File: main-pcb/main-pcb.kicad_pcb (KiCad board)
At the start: 10 copper layers, 118 x 90 mm, 443 parts, among them J1 CONN_01X03, J10 CONN_DUMPTRUCK_HOST, J11 CONN_01X03, J12 PMOD_HOST, J13 PMOD_HOST, J14 USB_C_Receptacle_USB2.0, J2 CORTEX_DEBUG_ETM, J3 XILINX_JTAG, J4 CORTEX_DEBUG_ETM, J5 CONN_01X03, J6 0826-1G1T-23-F, J7 CONN_DUMPTRUCK_HOST, J8 CONN_DUMPTRUCK_HOST, J9 CONN_DUMPTRUCK_HOST, M1 MECHANICAL, M2 SCREWHOLE, M3 SCREWHOLE, M4 SCREWHOLE, M5 SCREWHOLE, M6 MECHANICAL, M7 MECHANICAL, M8 MECHANICAL, M9 MECHANICAL, Q1 SSM6N58NU, SW1 SWITCH, SW2 SWITCH, U1 XC7S100-1FGGA484C, U10 NCP45525IMNTWG-H, U11 LTC3374-QFN, U12 AT24MAC402, U13 ECS-1612MV-250-CN, U14 STM32H735-UFBGA176-25, U15 S27KL0642GABHB020, U16 ECS-1612MV-250-CN, U17 S27KS0642GABHI030, U18 ECS-1612MV-250-CN, U19 INA230, U2 STM32L431-QFN48, U20 KSZ9031RN, U21 RCLAMP0514M, U22 RCLAMP0514M, U23 NCP45525IMNTWG-H, U24 IS25WP256D-JLLE, U25 INA230, U26 74LVC1T45, U27 NCP45525IMNTWG-H, U28 INA230, U29 NCP45525IMNTWG-H, U3 INA230, U30 INA230, U31 NCP45525IMNTWG-H, U32 INA230, U33 19-C47/RSGHBHC-5V01/2T, U34 19-C47/RSGHBHC-5V01/2T, U35 19-C47/RSGHBHC-5V01/2T, U36 19-C47/RSGHBHC-5V01/2T, U37 19-C47/RSGHBHC-5V01/2T, U38 19-C47/RSGHBHC-5V01/2T, U39 NCP45525IMNTWG-H, U4 INA230, U5 INA230, U6 INA230, U7 INA230, U8 INA230, U9 INA230

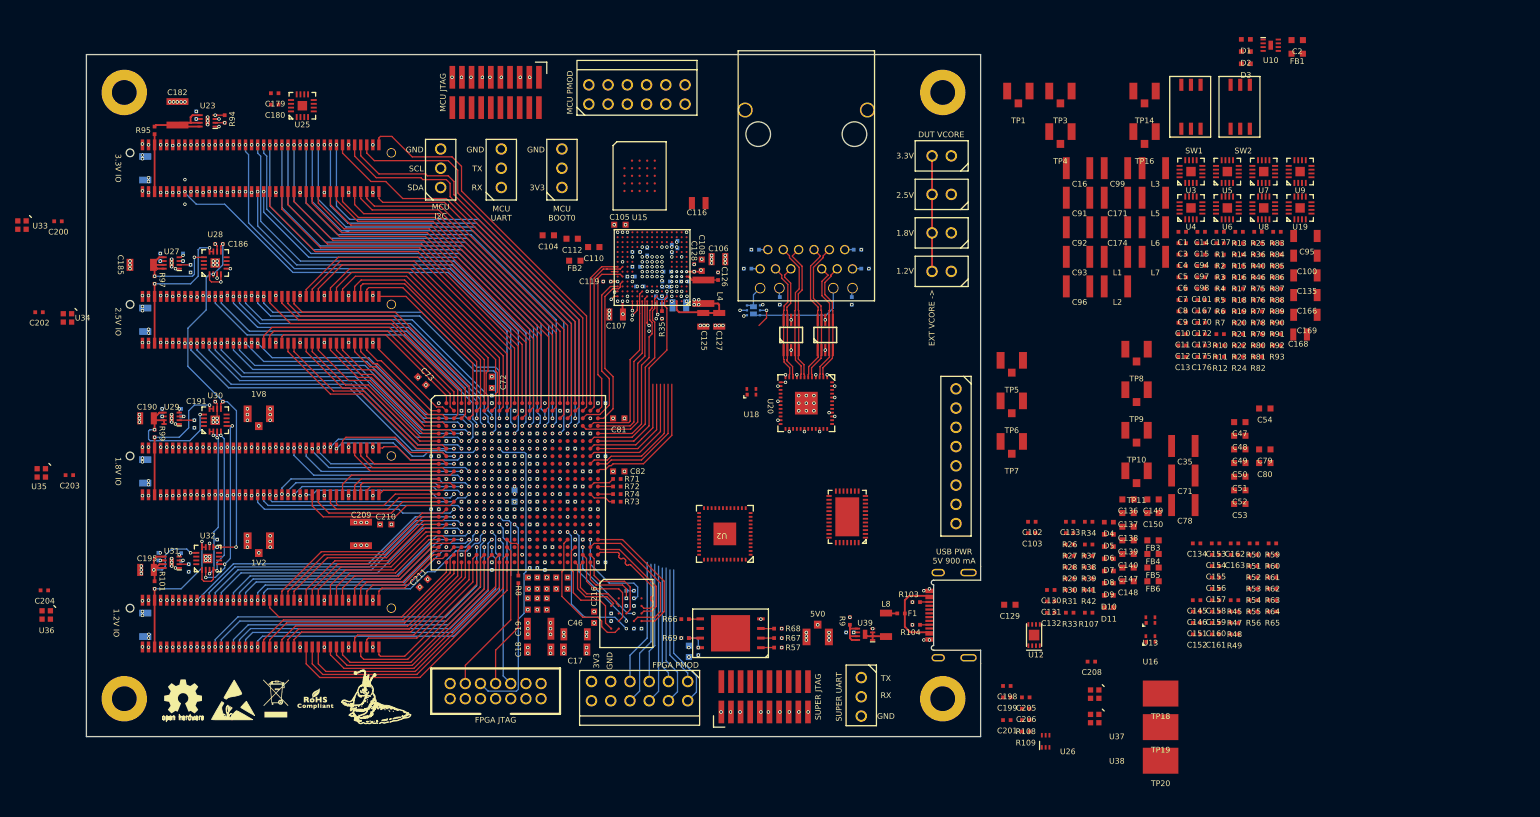
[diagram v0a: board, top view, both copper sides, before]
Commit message: Continued routing MCU, started work on PHY
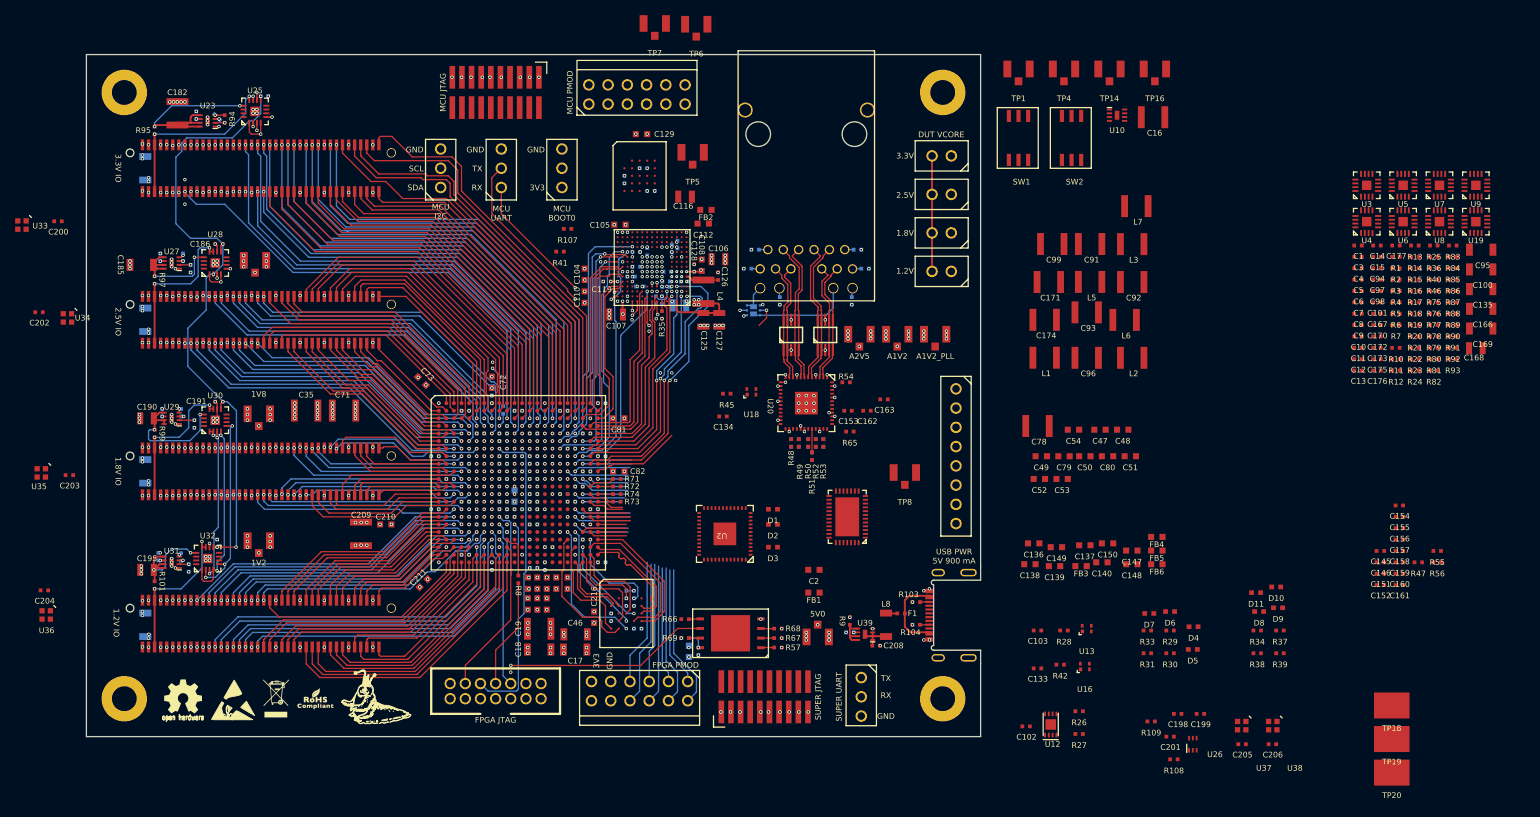
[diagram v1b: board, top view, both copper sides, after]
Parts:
- added R110: 33, azonenberg_pcb:EIA_0402_RES_NOSILK, B.Cu at (92.0, 72.9)
- C130, C131, C132, C179, C180, R59, R60, R61, R62, R63, R64: moved to B.Cu
- moved C35 115.8 mm to (66.0, 73.0), turned to 180 degrees
- moved C71 111.1 mm to (71.0, 73.0), turned to 180 degrees
- moved TP3 108.6 mm to (59.2, 53.2)
- moved FB1 95.5 mm to (133.0, 97.0)
- moved C2 94.6 mm to (133.0, 94.0)
- moved D3 89.2 mm to (127.6, 91.0)
- moved D2 88.2 mm to (127.6, 88.0)
- moved D1 88.0 mm to (127.6, 86.0)
- moved R107 85.4 mm to (100.5, 49.0)
- moved R41 82.0 mm to (99.5, 52.0)
- moved C131 79.1 mm to (108.0, 42.5), turned to 90 degrees
- moved C129 78.9 mm to (110.2, 36.5)
- moved C130 77.4 mm to (110.5, 41.0), turned to 180 degrees
- moved C132 76.7 mm to (111.5, 44.0)
- moved TP7 72.5 mm to (112.0, 22.0)
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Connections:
- U1 pad D9: /FLASH_SCK -> Net-(U1A-CCLK_0)
- U1 pad F17: /MCU/FMC_AD7 -> /MCU/FMC_AD11
- U1 pad F18: /MCU/FMC_NOE -> /MCU/FMC_AD14
- U1 pad F20: /MCU/FMC_AD13 -> /MCU/FMC_AD10
- U1 pad G17: /MCU/FMC_NBL0 -> /MCU/FMC_A17
- U1 pad G20: /MCU/FMC_A25 -> /MCU/FMC_AD13
- U1 pad G21: /MCU/FMC_A17 -> /MCU/FMC_NBL0
- U1 pad G22: /MCU/FMC_AD9 -> /MCU/FMC_A23
- U1 pad H18: /MCU/FMC_AD11 -> /MCU/FMC_AD7
- U1 pad H19: /MCU/FMC_AD10 -> /MCU/FMC_AD15
- U1 pad H20: /MCU/FMC_AD14 -> /MCU/FMC_NOE
- U1 pad H21: /MCU/FMC_AD15 -> /MCU/FMC_A19
- U1 pad J16: /MCU/FMC_A19 -> /MCU/FMC_A25
- U1 pad J19: /MCU/FMC_A20 -> /MCU/FMC_A22
- U1 pad J20: /MCU/FMC_A21 -> /MCU/FMC_AD9
- U1 pad J21: /MCU/FMC_A22 -> /MCU/FMC_A20
- U1 pad J22: /MCU/FMC_A23 -> /MCU/FMC_A21
- U1 pad P15: /Ethernet/ETH_MDIO -> unconnected-(U1E-IO_L13P_T2_MRCC_14-PadP15)
- U1 pad P16: /Ethernet/ETH_MDC -> unconnected-(U1E-IO_L13N_T2_MRCC_14-PadP16)
- U1 pad P17: /Ethernet/ETH_RST_N -> unconnected-(U1E-IO_L14P_T2_SRCC_14-PadP17)
- U1 pad R17: /Ethernet/ETH_LED2_N_1V8_INV -> unconnected-(U1E-IO_L16N_T2_D31_14-PadR17)
- U1 pad R18: unconnected-(U1E-IO_L14N_T2_SRCC_14-PadR18) -> /Ethernet/ETH_MDC
- U1 pad T19: unconnected-(U1E-IO_L18P_T2_D28_14-PadT19) -> /Ethernet/ETH_RST_N
- U1 pad T20: unconnected-(U1E-IO_L18N_T2_D27_14-PadT20) -> /Ethernet/ETH_LED2_N_1V8_INV
- U1 pad U17: /Ethernet/ETH_LED2_N_1V8 -> unconnected-(U1E-IO_L15N_T2_DQS_DOUT_CSO_B_14-PadU17)
- U1 pad U19: unconnected-(U1E-IO_L12N_T1_MRCC_14-PadU19) -> /Ethernet/ETH_MDIO
- U1 pad U20: unconnected-(U1E-IO_L11P_T1_SRCC_14-PadU20) -> /Ethernet/ETH_LED2_N_1V8
- U14 pad F15: /MCU/MCU_PMOD_DQ6 -> unconnected-(U14G-PG5-PadF15)
- U14 pad G12: /MCU/MCU_PMOD_DQ0 -> unconnected-(U14G-PG8-PadG12)
- U14 pad G13: /MCU/MCU_PMOD_DQ4 -> unconnected-(U14G-PG7-PadG13)
- U14 pad G14: /MCU/MCU_PMOD_DQ5 -> unconnected-(U14G-PG4-PadG14)
- U14 pad G15: /MCU/MCU_HYPERRAM_RST_N -> unconnected-(U14G-PG2-PadG15)
- U14 pad P10: unconnected-(U14B-PB11-PadP10) -> /MCU/MCU_PMOD_DQ0
- U14 pad P12: unconnected-(U14E-PE12-PadP12) -> /MCU/MCU_PMOD_DQ4
- U14 pad P13: unconnected-(U14E-PE13-PadP13) -> /MCU/MCU_PMOD_DQ5
- U14 pad R7: unconnected-(U14A-PA6-PadR7) -> /MCU/MCU_HYPERRAM_RST_N
- U14 pad R8: unconnected-(U14B-PB0-PadR8) -> /MCU/MCU_PMOD_DQ6
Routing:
- net /3V3: track 323.8 -> 442.5 mm, vias 45 -> 52
- net /GND: track 1304.7 -> 1400.8 mm, vias 388 -> 443
- net /FLASH_SCK: track 0.00 -> 72.9 mm, vias 1 -> 2
- net /MCU/FMC_A21: track 0.00 -> 36.1 mm, vias 1 -> 2
- net /MCU/FMC_A20: track 0.05 -> 33.6 mm, vias 1 -> 2
- net /3V3_SB: track 50.9 -> 84.0 mm, vias 7 -> 8
- net /MCU/FMC_AD11: track 0.00 -> 32.9 mm, vias 0 -> 2
- net /MCU/FMC_AD14: track 0.00 -> 30.9 mm, vias 0 -> 2
- net /MCU/FMC_AD13: track 0.00 -> 30.6 mm, vias 0 -> 2
- net /MCU/FMC_A19: track 0.05 -> 29.6 mm, vias 1 -> 2
- net /MCU/FMC_AD10: track 0.00 -> 28.8 mm, vias 0 -> 2
- net /MCU/FMC_NBL0: track 0.00 -> 27.9 mm
- net /SUPER_I2C_SDA: track 50.4 -> 78.3 mm, vias 4 -> 5
- net /MCU/MCU_UART_TX: track 1.02 -> 28.1 mm, vias 1 -> 2
- net /MCU/FMC_NOE: track 0.00 -> 26.7 mm, vias 1 -> 2
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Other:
- board text added: "A1V2"
- board text added: "A1V2_PLL"
- board text added: "A2V5"
- board text added: "FPGA"
- board text added: "LTC3374"
- board text added: "PHY"
- board text added: "Power infra"
- board text removed: "EXT VCORE ->"

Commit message: Continued routing MCU
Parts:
- C112, FB2, R107, R34, R37, R38, R39, R41: moved to B.Cu
- moved R39 112.0 mm to (104.2, 38.8)
- moved R38 108.9 mm to (104.2, 40.0)
- moved R37 108.9 mm to (104.2, 41.2)
- moved D9 106.1 mm to (105.2, 41.2), turned to 180 degrees
- moved R34 105.7 mm to (104.1, 42.5)
- moved D10 105.1 mm to (105.2, 40.0), turned to 180 degrees
- moved D11 104.0 mm to (105.2, 38.8), turned to 180 degrees
- moved D8 103.6 mm to (105.2, 42.5), turned to 180 degrees
- moved TP6 33.9 mm to (98.5, 50.2)
- moved C116 20.3 mm to (95.8, 46.7)
- moved TP7 20.0 mm to (117.2, 41.2)
- moved R41 16.3 mm to (110.0, 39.5), turned to -90 degrees
- moved R107 14.2 mm to (111.0, 39.5), turned to -90 degrees
- moved C112 3.32 mm to (115.2, 47.2), turned to 90 degrees
- moved TP5 2.51 mm to (117.2, 36.5)
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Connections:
- U1 pad G16: /MCU/FMC_AD8 -> /MCU/FMC_AD6
- U1 pad H18: /MCU/FMC_AD7 -> /MCU/FMC_AD9
- U1 pad J15: /MCU/FMC_AD1 -> /MCU/FMC_AD7
- U1 pad J16: /MCU/FMC_A25 -> /MCU/FMC_AD8
- U1 pad J17: /MCU/FMC_NBL1 -> /MCU/FMC_AD12
- U1 pad J19: /MCU/FMC_A22 -> /MCU/FMC_NBL1
- U1 pad J20: /MCU/FMC_AD9 -> /MCU/FMC_A16
- U1 pad K18: /MCU/FMC_AD12 -> /MCU/FMC_A25
- U1 pad K19: /MCU/FMC_AD6 -> /MCU/FMC_A22
- U1 pad K22: /MCU/FMC_A16 -> /MCU/FMC_AD1
- U14 pad L15: unconnected-(U14B-PB13-PadL15) -> /MCU/MCU_PMOD_DQ4
- U14 pad M1: /MCU/MCU_LED_0 -> unconnected-(U14C-PC2-PadM1)
- U14 pad M15: /MCU/MCU_PMOD_DQ2 -> /MCU/MCU_PMOD_DQ0
- U14 pad M2: unconnected-(U14C-PC3-PadM2) -> /PRSNT_1V2
- U14 pad M7: /MCU/MCU_PMOD_DQ3 -> unconnected-(U14C-PC5-PadM7)
- U14 pad N12: unconnected-(U14B-PB10-PadN12) -> /MCU/MCU_LED_3
- U14 pad N13: unconnected-(U14H-PH8-PadN13) -> /MCU/MCU_LED_0
- U14 pad N14: unconnected-(U14H-PH10-PadN14) -> /MCU/MCU_PMOD_DQ5
- U14 pad N15: /MCU/MCU_LED_2 -> /MCU/MCU_PMOD_DQ1
- U14 pad P10: /MCU/MCU_PMOD_DQ0 -> unconnected-(U14B-PB11-PadP10)
- U14 pad P11: /MCU/MCU_LED_1 -> unconnected-(U14F-PF12-PadP11)
- U14 pad P12: /MCU/MCU_PMOD_DQ4 -> /MCU/MCU_LED_2
- U14 pad P13: /MCU/MCU_PMOD_DQ5 -> /MCU/MCU_LED_1
- U14 pad P15: /MCU/MCU_LED_3 -> /MCU/MCU_PMOD_DQ6
- U14 pad P5: /PRSNT_1V2 -> /MCU/MCU_PMOD_DQ3
- U14 pad R10: /MCU/MCU_PMOD_DQ1 -> unconnected-(U14F-PF14-PadR10)
- U14 pad R4: unconnected-(U14H-PH3-PadR4) -> /MCU/MCU_PMOD_DQ7
- U14 pad R6: /MCU/MCU_PMOD_DQ7 -> /MCU/MCU_PMOD_DQ2
- U14 pad R8: /MCU/MCU_PMOD_DQ6 -> unconnected-(U14B-PB0-PadR8)
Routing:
- net /3V3_SB: track 84.0 -> 174.5 mm, vias 8 -> 10
- net /1V8: track 172.5 -> 247.7 mm
- net /GND: track 1400.8 -> 1466.1 mm, vias 443 -> 474
- net /2V5: track 98.3 -> 160.9 mm
- net /3V3: track 442.5 -> 503.3 mm, vias 52 -> 57
- net Net-(J11-P2): track 0.00 -> 47.3 mm, vias 0 -> 1
- net /MCU/FMC_AD5: track 0.00 -> 47.2 mm, vias 1 -> 2
- net /MCU/FMC_AD7: track 0.00 -> 46.8 mm, vias 1 -> 2
- net /MCU/FMC_AD4: track 0.00 -> 43.0 mm, vias 1 -> 2
- net /MCU/FMC_AD8: track 0.00 -> 40.9 mm, vias 1 -> 2
- net /MCU/MCU_RST_N: track 0.00 -> 38.5 mm, vias 0 -> 3
- net /MCU/MCU_JTAG_TDO: track 11.8 -> 49.8 mm, vias 1 -> 2
- net /MCU/FMC_AD9: track 6.50 -> 43.1 mm, vias 1 -> 2
- net /I2C_SDA: track 126.8 -> 161.7 mm, vias 4 -> 5
- net /MCU/FMC_A25: track 0.00 -> 33.9 mm
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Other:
- board text added: "2V5"
- board text added: "VCORE"
- board text added: "VDDA"
- board text added: "VSMPS"

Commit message: 500 unrouted, still lots more to go
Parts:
- C103, C145, C146, C151, C152, C153, C154, C156, C157, C158, C159, C160, C161, C162, C163, R26, R27: moved to B.Cu
- moved R27 129.3 mm to (70.8, 30.5), turned to 90 degrees
- moved R26 127.7 mm to (69.8, 31.0), turned to 90 degrees
- moved C102 124.5 mm to (68.5, 31.2), turned to 180 degrees
- moved U12 124.4 mm to (69.8, 33.5)
- moved C160 84.6 mm to (128.8, 71.8)
- moved C158 84.1 mm to (129.2, 68.8), turned to -90 degrees
- moved C157 83.0 mm to (128.8, 74.2)
- moved C151 81.8 mm to (129.5, 70.8)
- moved C159 80.7 mm to (133.2, 68.8), turned to -90 degrees
- moved C152 80.5 mm to (130.0, 75.2), turned to 90 degrees
- moved C161 79.5 mm to (135.2, 69.8), turned to 180 degrees
- moved C146 78.3 mm to (131.5, 75.4), turned to 90 degrees
- moved C156 77.3 mm to (134.5, 73.2), turned to 180 degrees
- moved C154 76.3 mm to (135.2, 71.2), turned to 180 degrees
- moved C145 75.8 mm to (133.8, 75.3), turned to 90 degrees
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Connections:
- R65 pad 1: /3V3 -> /1V8
- U1 pad K16: /MCU/FPGA_PMOD_DQ1 -> /MCU/FPGA_PMOD_DQ4
- U1 pad K17: /MCU/FPGA_LED_2 -> /MCU/FPGA_PMOD_DQ0
- U1 pad L15: /MCU/FPGA_PMOD_DQ7 -> /MCU/FPGA_LED_0
- U1 pad L16: /MCU/FPGA_LED_3 -> /MCU/FPGA_LED_1
- U1 pad L18: /MCU/FPGA_PMOD_DQ2 -> /MCU/FPGA_PMOD_DQ5
- U1 pad L19: /MCU/FPGA_PMOD_DQ3 -> /MCU/FPGA_PMOD_DQ7
- U1 pad L20: /MCU/FPGA_PMOD_DQ4 -> /MCU/FPGA_PMOD_DQ2
- U1 pad L21: /MCU/FPGA_PMOD_DQ5 -> /MCU/FPGA_PMOD_DQ6
- U1 pad L22: /MCU/FPGA_PMOD_DQ0 -> /MCU/FPGA_PMOD_DQ1
- U1 pad M16: /MCU/FPGA_PMOD_DQ6 -> /MCU/FPGA_LED_2
- U1 pad M17: /MCU/FPGA_LED_0 -> /MCU/FPGA_LED_3
- U1 pad M18: /MCU/FPGA_LED_1 -> /MCU/FPGA_PMOD_DQ3
- U1 pad R20: /Ethernet/ETH_LED1_N_1V8 -> /Ethernet/ETH_LED2_N_1V8
- U1 pad T22: /Ethernet/RGMII_TXD1 -> /Ethernet/ETH_LED1_N_1V8
- U1 pad U20: /Ethernet/ETH_LED2_N_1V8 -> /Ethernet/RGMII_TX_EN
- U1 pad U22: /Ethernet/RGMII_TX_CLK -> /Ethernet/RGMII_TXD1
- U1 pad V20: /Ethernet/RGMII_TXD3 -> /Ethernet/RGMII_TXD2
- U1 pad V21: /Ethernet/RGMII_TXD2 -> /Ethernet/RGMII_TX_CLK
- U1 pad V22: /Ethernet/RGMII_TX_EN -> /Ethernet/RGMII_TXD3
- U14 pad B10: unconnected-(U14D-PD2-PadB10) -> /PRSNT_1V2
- U14 pad B11: unconnected-(U14C-PC12-PadB11) -> /PRSNT_1V8
- U14 pad C12: unconnected-(U14C-PC10-PadC12) -> /PRSNT_3V3
- U14 pad C13: unconnected-(U14H-PH13-PadC13) -> /PRSNT_2V5
- U14 pad C14: unconnected-(U14A-PA10-PadC14) -> /FPGA_DONE
- U14 pad M2: /PRSNT_1V2 -> unconnected-(U14C-PC3-PadM2)
- U14 pad N5: /PRSNT_1V8 -> unconnected-(U14A-PA3-PadN5)
- U14 pad P1: /FPGA_DONE -> unconnected-(U14A-PA0-PadP1)
- U14 pad P2: /PRSNT_3V3 -> unconnected-(U14A-PA1-PadP2)
- U14 pad R2: /PRSNT_2V5 -> unconnected-(U14A-PA2-PadR2)
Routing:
- net /GND: track 1466.1 -> 1557.0 mm, vias 474 -> 509
- net /Ethernet/FPGA_FLASH_CS_N: track 1.73 -> 43.8 mm, vias 0 -> 2
- net /Ethernet/FPGA_FLASH_DQ2: track 0.00 -> 38.6 mm, vias 1 -> 2
- net /Ethernet/FPGA_FLASH_DQ1: track 0.00 -> 38.4 mm, vias 1 -> 2
- net /Ethernet/ETH_LED2_N_1V8: track 6.21 -> 40.4 mm, vias 1 -> 0
- net /Ethernet/RGMII_TXD2: track 4.96 -> 38.6 mm
- net /Ethernet/RGMII_TX_CLK: track 3.75 -> 36.5 mm
- net /Ethernet/RGMII_TXD0: track 5.46 -> 38.2 mm
- net /Ethernet/RGMII_TXD1: track 4.25 -> 36.7 mm
- net /Ethernet/ETH_LED1_N_1V8: track 6.21 -> 37.5 mm
- net /Ethernet/RGMII_TXD3: track 5.96 -> 36.1 mm
- net /Ethernet/FPGA_FLASH_DQ3: track 0.00 -> 28.2 mm, vias 1 -> 3
- net /PRSNT_3V3: track 85.7 -> 113.6 mm, vias 1 -> 2
- net /PRSNT_2V5: track 64.7 -> 92.1 mm, vias 1 -> 2
- net /PRSNT_1V8: track 39.6 -> 66.6 mm, vias 1 -> 2
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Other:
- board text added: "0"
- board text added: "1"
- board text added: "2"
- board text added: "3"
- board text added: "FPGA LED"
- board text added: "MCU LED"

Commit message: Began routing supervisor
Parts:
- C1, C3, C53, C6, C7, FB1, R1, R36, R40, R5, R56, R6, R7: moved to B.Cu
- moved R40 163.8 mm to (54.4, 87.6)
- moved R36 163.2 mm to (56.5, 92.2), turned to 180 degrees
- moved TP18 145.5 mm to (65.5, 89.5)
- moved R1 102.1 mm to (125.5, 110.2), turned to 90 degrees
- moved R7 98.9 mm to (118.0, 98.6), turned to 90 degrees
- moved R6 98.8 mm to (118.8, 98.6), turned to 90 degrees
- moved R5 97.9 mm to (120.5, 98.8), turned to -90 degrees
- moved C3 96.6 mm to (126.5, 109.2), turned to -90 degrees
- moved C7 96.0 mm to (116.6, 96.5), turned to 90 degrees
- moved C8 92.4 mm to (117.1, 89.4)
- moved C1 92.3 mm to (121.6, 91.2), turned to 180 degrees
- moved R55 92.2 mm to (125.5, 70.2), turned to -90 degrees
- moved C6 91.5 mm to (122.6, 97.3), turned to -90 degrees
- moved C4 91.4 mm to (124.0, 97.0), turned to -90 degrees
- moved R47 91.1 mm to (124.5, 70.2), turned to -90 degrees
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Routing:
- net /3V3_SB: track 172.6 -> 238.6 mm, vias 10 -> 20
- net /GND: track 1557.0 -> 1620.4 mm, vias 509 -> 537
- net /MCU/SUPER_SPI_MOSI: track 18.4 -> 47.8 mm, vias 1 -> 2
- net /MCU/SUPER_SPI_MISO: track 18.8 -> 48.3 mm, vias 1 -> 2
- net /MCU/SUPER_SPI_SCK: track 14.4 -> 42.2 mm, vias 1 -> 2
- net /MCU/SUPER_SPI_CS_N: track 11.9 -> 39.4 mm, vias 1 -> 2
- net /Power supply/SUPER_RST_N: track 0.00 -> 19.0 mm, vias 0 -> 2
- net /Power supply/SUPER_JTAG_TMS: track 0.00 -> 18.9 mm, vias 0 -> 2
- net /Power supply/SUPER_JTAG_TDO: track 0.00 -> 16.1 mm, vias 0 -> 2
- net /1V8: track 264.1 -> 279.9 mm, vias 51 -> 56
- net /Power supply/SUPER_JTAG_TDI: track 0.00 -> 14.6 mm, vias 0 -> 2
- net /1V0: track 75.6 -> 90.2 mm
- net /Power supply/SUPER_JTAG_TCK: track 0.00 -> 14.0 mm, vias 0 -> 2
- net /Ethernet/ETH_CLK_25MHZ: track 0.00 -> 3.35 mm
- net /MCU/MCU_HYPERRAM_DQ7: track 27.8 -> 24.5 mm
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
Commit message: Under 400 unrouted
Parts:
- C133, R42: moved to B.Cu
- moved U16 66.8 mm to (100.2, 99.8), turned to 90 degrees
- moved R42 64.1 mm to (99.8, 98.5), turned to -90 degrees
- moved C133 60.1 mm to (100.8, 99.8), turned to 90 degrees
- moved U36 56.3 mm to (41.2, 44.5)
- moved C155 53.3 mm to (135.2, 67.8)
- moved C204 51.8 mm to (42.2, 46.0)
- moved U33 50.1 mm to (41.2, 97.0)
- moved C200 50.0 mm to (43.2, 97.0), turned to 90 degrees
- moved TP20 33.1 mm to (198.0, 77.1)
- moved TP19 33.1 mm to (198.0, 72.7)
- moved C202 28.2 mm to (42.2, 85.8)
- moved U34 24.5 mm to (41.2, 84.2)
- moved C15 23.6 mm to (194.5, 100.8)
- moved U9 23.6 mm to (198.0, 100.1)
- moved U35 19.1 mm to (41.2, 65.0)
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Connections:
- U2 pad 33: /Power supply/SUPER_FAULT_LED -> /DUT_VCCIO_EN
- U2 pad 45: /DUT_VCCIO_EN -> /Power supply/SUPER_FAULT_LED
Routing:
- net /VBUS_SHOUT: track 4.66 -> 184.3 mm, vias 2 -> 7
- net /GND: track 1620.4 -> 1716.8 mm, vias 537 -> 547
- net /3V3_SB: track 238.6 -> 309.9 mm, vias 20 -> 24
- net /INA_ALERT: track 67.0 -> 114.2 mm
- net /SUPER_I2C_SDA: track 78.3 -> 125.0 mm
- net /SUPER_I2C_SCL: track 71.0 -> 116.5 mm
- net /DUT_VCCIO_EN: track 111.2 -> 153.1 mm, vias 6 -> 7
- net /Power supply/SUPER_UART_TX: track 0.00 -> 38.6 mm, vias 0 -> 1
- net /Power supply/SUPER_UART_RX: track 0.00 -> 34.4 mm, vias 0 -> 1
- net /PRSNT_3V3: track 113.6 -> 142.6 mm, vias 2 -> 3
- net /PRSNT_2V5: track 92.1 -> 120.5 mm, vias 2 -> 3
- net /PRSNT_1V8: track 66.6 -> 92.8 mm, vias 2 -> 3
- net /PRSNT_1V2: track 44.0 -> 68.0 mm, vias 2 -> 3
- net /I2C_SDA: track 186.5 -> 209.2 mm, vias 6 -> 7
- net /I2C_SCL: track 186.0 -> 208.4 mm, vias 7 -> 8
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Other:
- board size 118 x 90 mm -> 130 x 90 mm
- board text added: "PWR"
- board text added: "Place UL mark and date code in this area"
- board text added: "RST"
